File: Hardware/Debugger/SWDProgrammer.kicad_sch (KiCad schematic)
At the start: 37 parts, among them J1 USB_C_Receptacle_USB2.0, J2 USB_C_Receptacle_USB2.0, U1 AP2112K-3.3, U2 STM32F103C8Tx, Y1 32.768KHZ, Y2 8Mhz

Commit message: new debugger
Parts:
- removed U41: ~, Library:BK13C06-10DP, symbol Library:BK13C06-10D(S/P)
- added U4: Conn_01x14_Socket, Library:FPC, symbol Connector:Conn_01x14_Socket
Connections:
- net 5V(2): now also U4.3 (Pin_3)
- net D+: now also U4.10 (Pin_10)
- net D-: now also U4.11 (Pin_11)
- net GND: now also U4.4 (Pin_4), U4.5 (Pin_5)
- net RESET: now also U4.9 (Pin_9)
- net SCL: now also U4.6 (Pin_6)
- net SDA: now also U4.7 (Pin_7)
- net VDD_nRF: now also U4.8 (Pin_8)
- net swc: now also U4.13 (Pin_13)
- net swd: now also U4.12 (Pin_12)
- new net Batteryin: U4.1 (Pin_1), U4.2 (Pin_2)
- no-connect marks 8 -> 9
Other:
- note added: "Battery + header"

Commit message: current version
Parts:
- added JP6: Jumper_2_Open, Jumper:SolderJumper-2_P1.3mm_Open_RoundedPad1.0x1.5mm, symbol Jumper:Jumper_2_Open
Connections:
- net A10: now also JP6.2 (B)
- net A9: now also JP6.1 (A)
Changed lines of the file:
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@@
+		)
+	)
+	(label "A9"
+		(at 97.79 59.055 180)
+		(fields_autoplaced yes)
+		(effects
+			(font
+				(size 1.27 1.27)
+			)
+			(justify right bottom)
 		)
 	)
@@
 	(label "OSCOUT"
 		(at 149.225 33.655 0)
+		(fields_autoplaced yes)
+		(effects
+			(font
+				(size 1.27 1.27)
+			)
+			(justify left bottom)
+		)
+	)
+	(label "A10"
+		(at 107.95 59.055 0)
 		(fields_autoplaced yes)
 		(effects
@@
 					(unit 1)
 				)
+			)
+		)
+	)
+	(symbol
+		(lib_id "Jumper:Jumper_2_Open")
+		(at 102.87 59.055 0)
+		(unit 1)
+		(exclude_from_sim no)
+		(in_bom yes)
+		(on_board yes)
+		(dnp no)
+		(fields_autoplaced yes)
+		(property "Reference" "JP6"
+			(at 102.87 53.34 0)
+			(effects
+				(font
+					(size 1.27 1.27)
+				)
+			)
+		)
+		(property "Value" "Jumper_2_Open"
+			(at 102.87 55.88 0)
+			(effects
+				(font
+					(size 1.27 1.27)
+				)
+			)
+		)
+		(property "Footprint" "Jumper:SolderJumper-2_P1.3mm_Open_RoundedPad1.0x1.5mm"
+			(at 102.87 59.055 0)
+			(effects
+				(font
+					(size 1.27 1.27)
+				)
+				(hide yes)
+			)
+		)
+		(property "Datasheet" "~"
+			(at 102.87 59.055 0)
+			(effects
+				(font
+					(size 1.27 1.27)
+				)
+				(hide yes)
+			)
+		)
+		(property "Description" ""
+			(at 102.87 59.055 0)
+			(effects
+				(font
+					(size 1.27 1.27)
+				)
+				(hide yes)
+			)
+		)
+		(pin "1"
+		)
+		(pin "2"
+		)
+		(instances
+			(project "SWDProgrammer"
+				(path "/c10d4a68-1c04-4145-8c29-cc9b9e805c41"
+					(reference "JP6")
+					(unit 1)
+				)

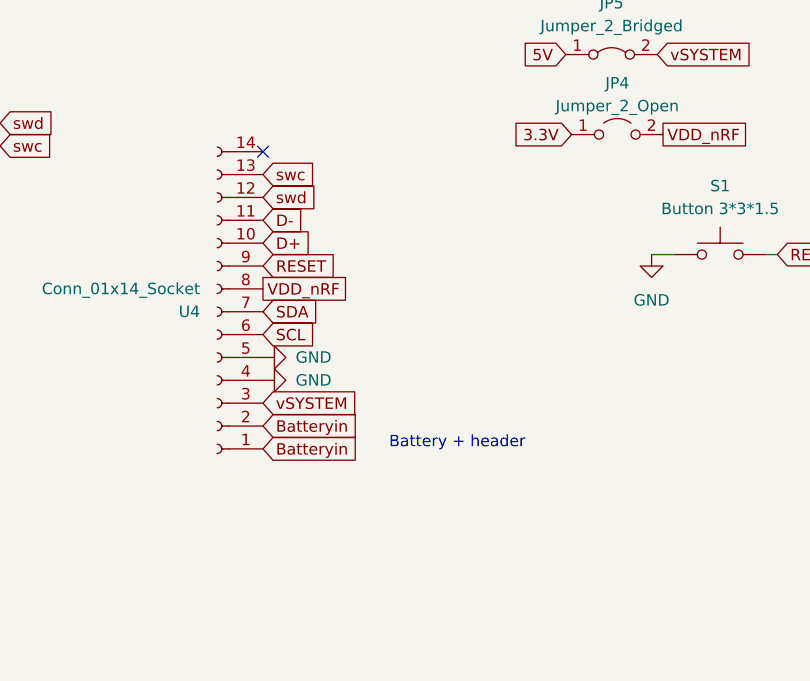
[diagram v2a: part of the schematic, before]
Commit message: added gyro, flex pcb antenna
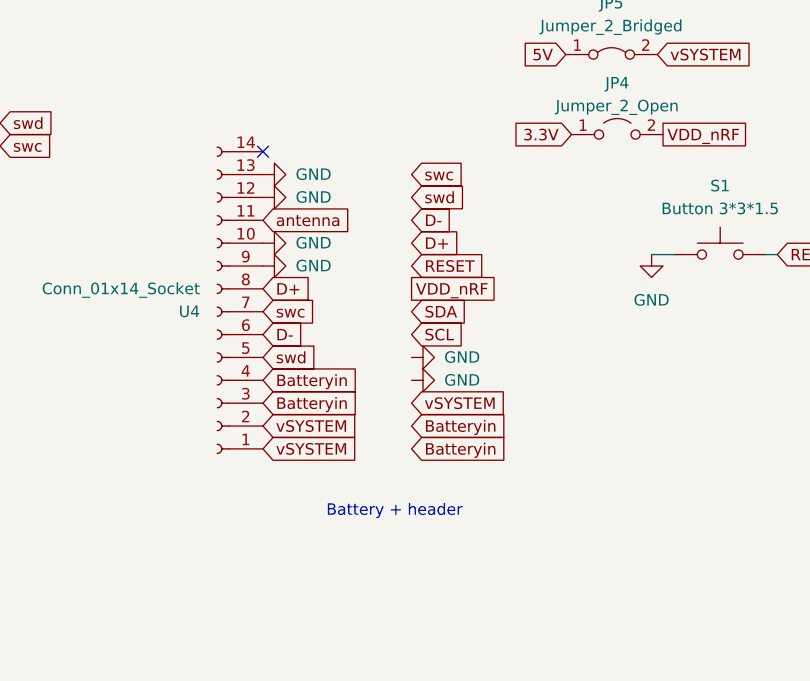
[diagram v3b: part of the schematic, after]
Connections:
- net 5V(2): now also U4.1 (Pin_1), U4.2 (Pin_2); no longer U4.3 (Pin_3)
- net Batteryin: now also U4.3 (Pin_3), U4.4 (Pin_4); no longer U4.1 (Pin_1), U4.2 (Pin_2)
- net D+: now also U4.8 (Pin_8); no longer U4.10 (Pin_10)
- net D-: now also U4.6 (Pin_6); no longer U4.11 (Pin_11)
- net GND: now also U4.10 (Pin_10), U4.12 (Pin_12), U4.13 (Pin_13), U4.9 (Pin_9); no longer U4.4 (Pin_4), U4.5 (Pin_5)
- net RESET: no longer U4.9 (Pin_9)
- net SCL: no longer U4.6 (Pin_6)
- net SDA: no longer U4.7 (Pin_7)
- net VDD_nRF: no longer U4.8 (Pin_8)
- net swc: now also U4.7 (Pin_7); no longer U4.13 (Pin_13)
- net swd: now also U4.5 (Pin_5); no longer U4.12 (Pin_12)
- new net antenna: U4.11 (Pin_11)

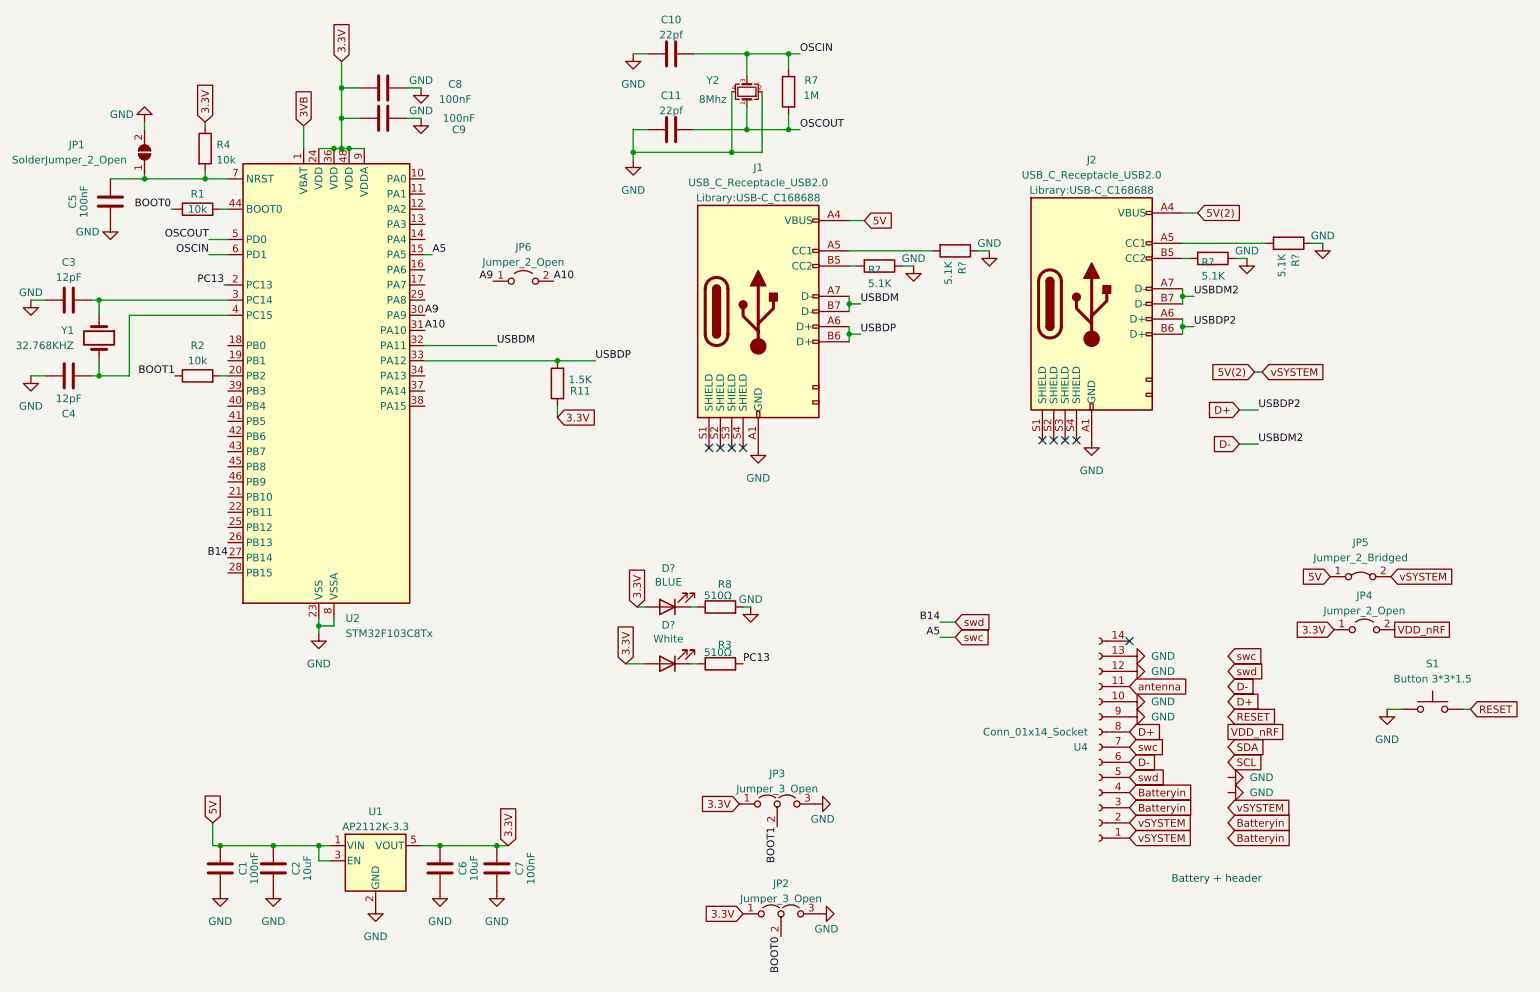
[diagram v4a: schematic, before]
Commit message: revolute production boards
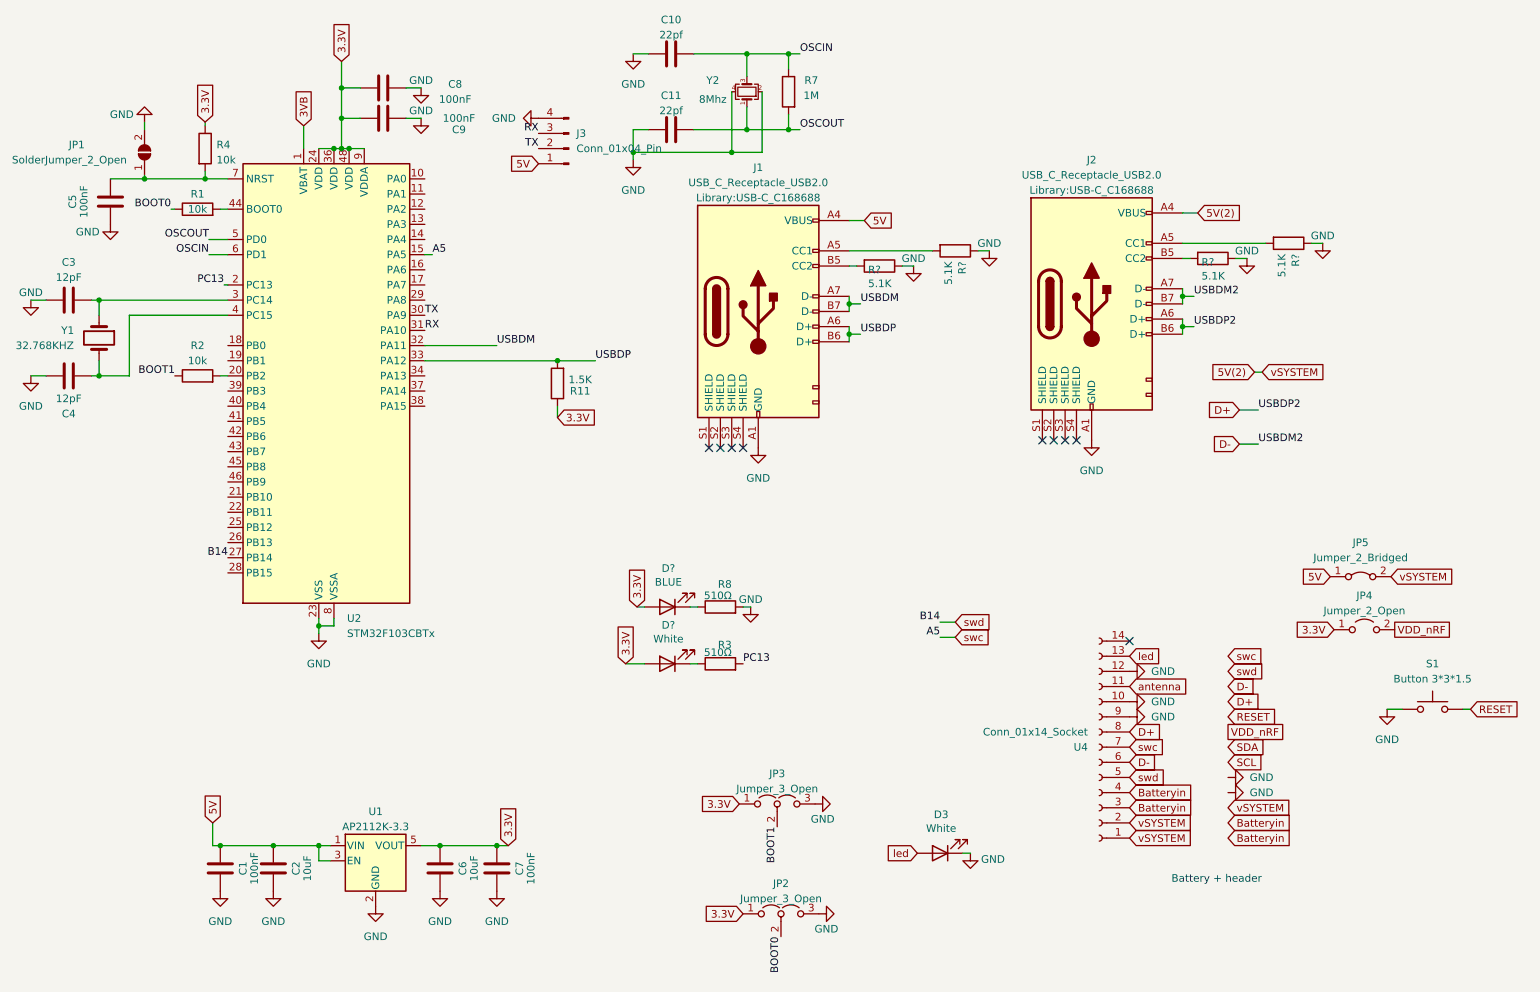
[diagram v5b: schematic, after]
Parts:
- removed JP6: Jumper_2_Open, Jumper:SolderJumper-2_P1.3mm_Open_RoundedPad1.0x1.5mm, symbol Jumper:Jumper_2_Open
- removed U2: STM32F103C8Tx, Package_QFP:LQFP-48_7x7mm_P0.5mm, symbol MCU_ST_STM32F1:STM32F103C8Tx
- added D3: White, LED_SMD:LED_0402_1005Metric, symbol Device:LED
- added J3: Conn_01x04_Pin, Connector_PinHeader_1.27mm:PinHeader_1x04_P1.27mm_Vertical, symbol Connector:Conn_01x04_Pin
- added U2: STM32F103CBTx, Package_QFP:LQFP-48_7x7mm_P0.5mm, symbol MCU_ST_STM32F1:STM32F103CBTx
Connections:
- net 3.3V: now also U2.24 (VDD), U2.36 (VDD), U2.48 (VDD), U2.9 (VDDA)
- net 3VB: now also U2.1 (VBAT)
- net 5V: now also J3.1 (Pin_1)
- net GND: now also D3.1 (K), J3.4 (Pin_4), U2.23 (VSS), U2.35 (VSS), U2.47 (VSS), U2.8 (VSSA); no longer U4.13 (Pin_13)
- net OSCIN: now also U2.6 (PD1)
- net OSCOUT: now also U2.5 (PD0)
- net PC13: now also U2.2 (PC13)
- net USBDM: now also U2.32 (PA11)
- net USBDP: now also U2.33 (PA12)
- net swc: now also U2.15 (PA5)
- net swd: now also U2.27 (PB14)
- net at C5.2, JP1.1 (A), R4.2: now also U2.7 (NRST)
- net at C3.2, Y1.1: now also U2.3 (PC14)
- net at C4.1, Y1.2: now also U2.4 (PC15)
- net at R1.2: now also U2.44 (BOOT0)
- net at R2.2: now also U2.20 (PB2)
- new net RX: J3.3 (Pin_3), U2.31 (PA10)
- new net TX: J3.2 (Pin_2), U2.30 (PA9)
- new net led: D3.2 (A), U4.13 (Pin_13)
